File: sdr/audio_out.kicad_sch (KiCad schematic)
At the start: 8 parts, among them J4 AudioJack4, U3 LM4871M/TR_C383075

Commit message: First version 0.1 completed
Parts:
- C4: value 390n -> 330n
- J4: value AudioJack4 -> PJ-320D
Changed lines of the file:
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@@
       (effects (font (size 1.27 1.27)) (justify right))
     )
-    (property "Value" "AudioJack4" (at 224.79 81.9149 0)
+    (property "Value" "PJ-320D" (at 224.79 81.9149 0)
       (effects (font (size 1.27 1.27)) (justify right))
     )
@@
       (effects (font (size 1.27 1.27)))
     )
-    (property "Value" "390n" (at 87.63 80.01 90)
+    (property "Value" "330n" (at 87.63 80.01 90)
       (effects (font (size 1.27 1.27)))
     )

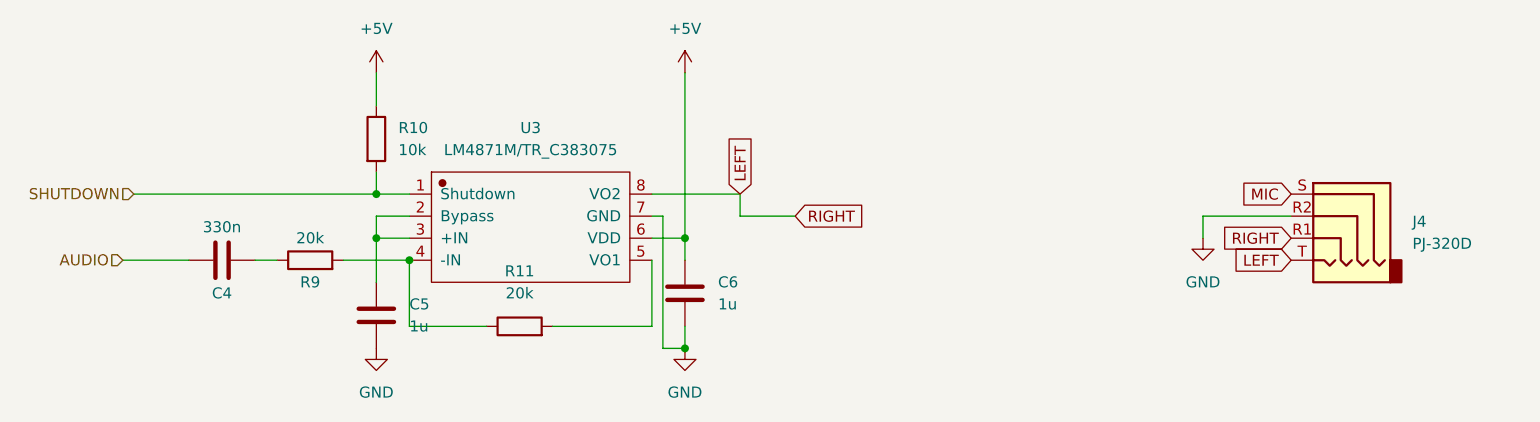
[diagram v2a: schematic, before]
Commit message: Convert to a 4-layer board.
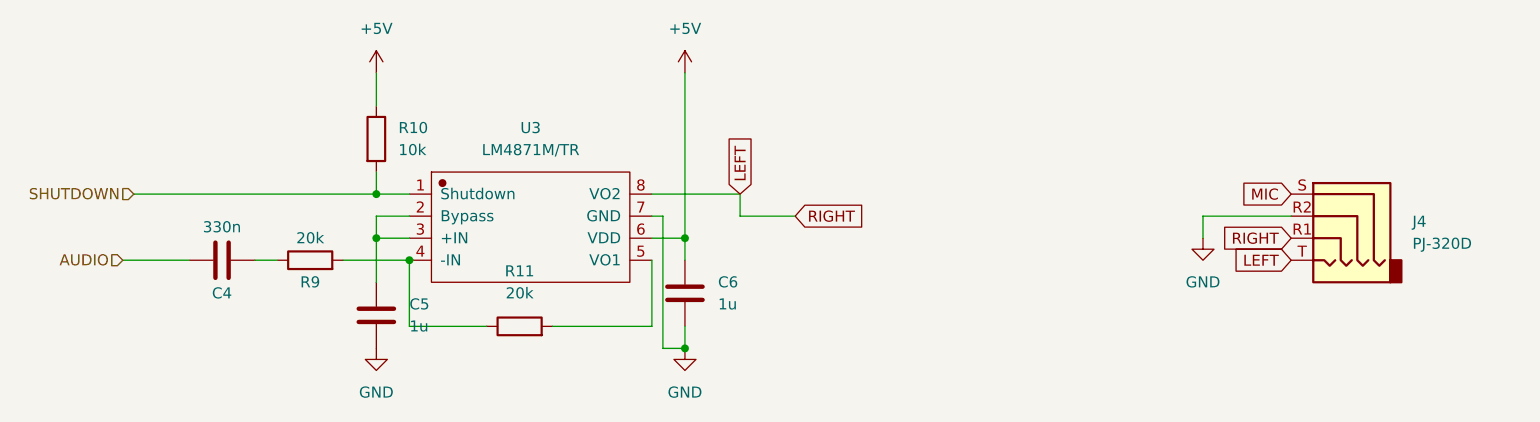
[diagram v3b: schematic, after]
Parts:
- U3: value LM4871M/TR_C383075 -> LM4871M/TR; SuppliersPartNumber C383075 -> (none); uuid std:36ae7e920fbc4175b27029281f17c4a6 -> (none)
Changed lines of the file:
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@@
       (effects (font (size 1.27 1.27)))
     )
-    (property "Value" "LM4871M/TR_C383075" (at 123.19 71.12 0)
+    (property "Value" "LM4871M/TR" (at 123.19 71.12 0)
       (effects (font (size 1.27 1.27)))
     )
@@
       (effects (font (size 1.27 1.27)) hide)
     )
-    (property "SuppliersPartNumber" "C383075" (at 123.19 85.09 0)
-      (effects (font (size 1.27 1.27)) hide)
-    )
-    (property "uuid" "std:36ae7e920fbc4175b27029281f17c4a6" (at 123.19 88.9 0)
-      (effects (font (size 1.27 1.27)) hide)
-    )

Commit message: Update footprints, and add an swd-connect-5
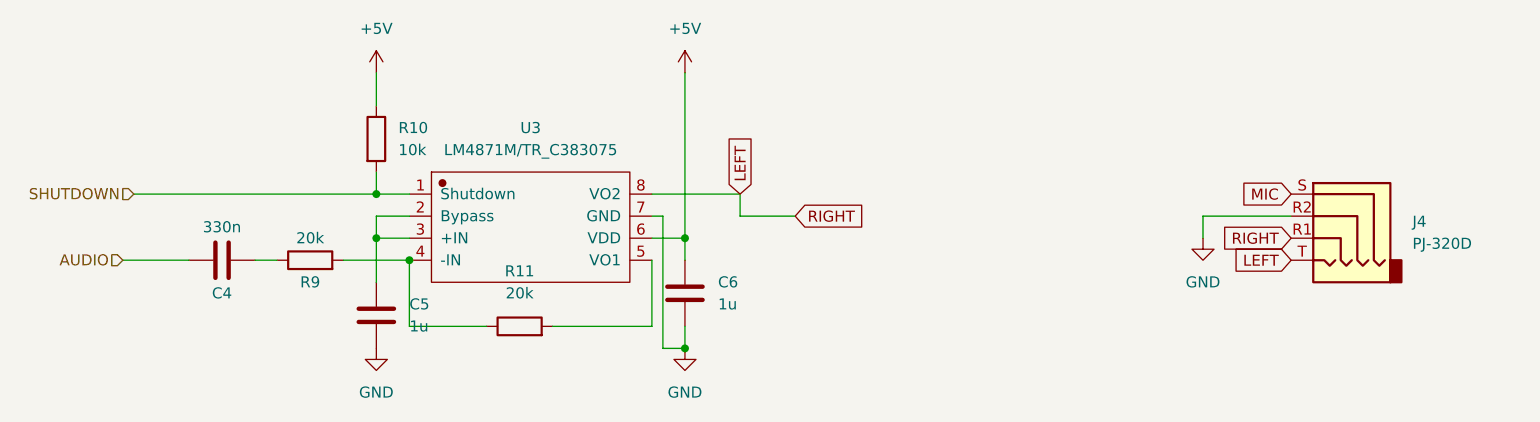
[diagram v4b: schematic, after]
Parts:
- U3: value LM4871M/TR -> LM4871M/TR_C383075; symbol zl4aa:LM4871M/TR_C383075 -> zl4aa:LM4871M/TR_C383075; SuppliersPartNumber (none) -> C383075; uuid (none) -> std:36ae7e920fbc4175b27029281f17c4a6
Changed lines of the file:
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@@
     )
   )
-  (symbol (lib_id "zl4aa:LM4871M{slash}TR_C383075") (at 123.19 80.01 0) (unit 1)
+  (symbol (lib_id "zl4aa:LM4871M/TR_C383075") (at 123.19 80.01 0) (unit 1)
     (in_bom yes) (on_board yes) (dnp no) (fields_autoplaced)
     (property "Reference" "U3" (at 123.19 68.58 0)
       (effects (font (size 1.27 1.27)))
     )
-    (property "Value" "LM4871M/TR" (at 123.19 71.12 0)
+    (property "Value" "LM4871M/TR_C383075" (at 123.19 71.12 0)
       (effects (font (size 1.27 1.27)))
     )
@@
       (effects (font (size 1.27 1.27)) hide)
     )
+    (property "SuppliersPartNumber" "C383075" (at 123.19 85.09 0)
+      (effects (font (size 1.27 1.27)) hide)
+    )
+    (property "uuid" "std:36ae7e920fbc4175b27029281f17c4a6" (at 123.19 88.9 0)
+      (effects (font (size 1.27 1.27)) hide)
+    )
